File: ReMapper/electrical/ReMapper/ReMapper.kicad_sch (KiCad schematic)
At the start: 50 parts, among them J1 QSPI_Debug, J2 USB_IN, J3 USB_IN_Debug, J4 ESP_UART0, J5 USB_OUT, J6 USB_OUT_Debug, U1 ESP32-S3-WROOM-1-N8R8, U2 RP2040, U3 W25Q128JVE, U4 RT6150B-33GQW, U5 W25Q128JVE, Y1 12MHZ

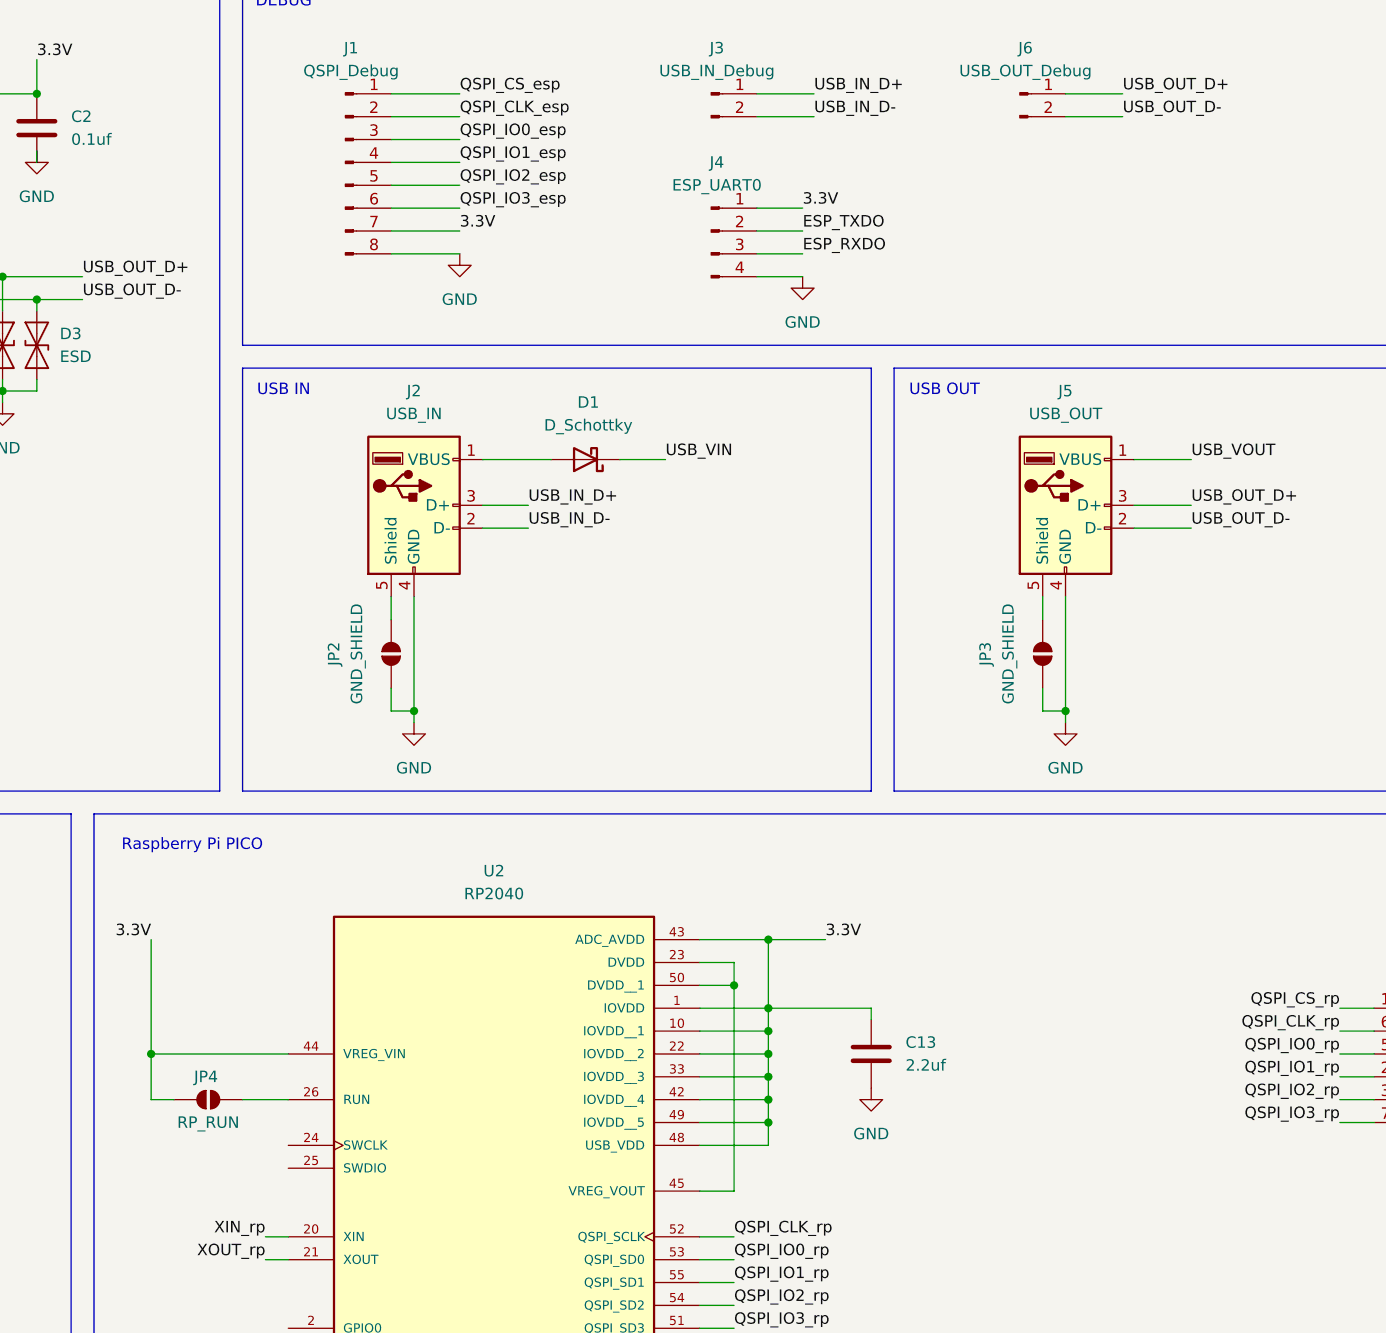
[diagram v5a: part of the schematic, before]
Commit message: split he layout a little
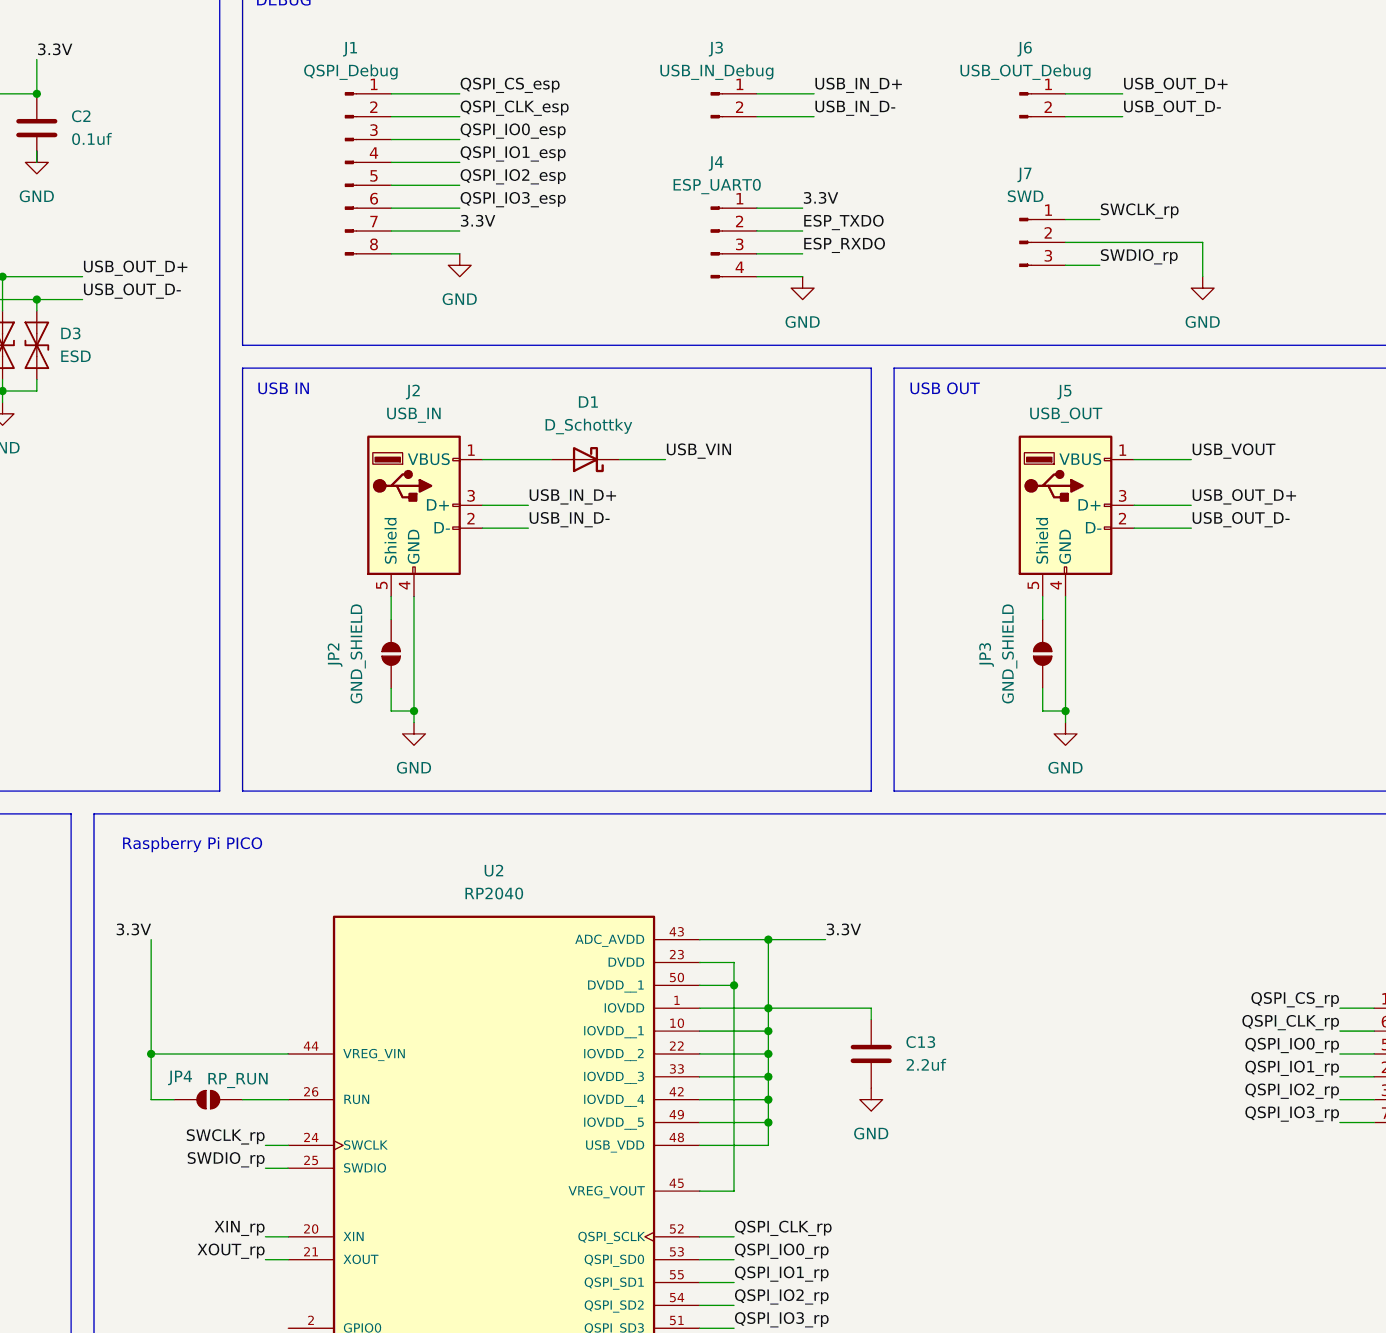
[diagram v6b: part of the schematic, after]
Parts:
- added J7: SWD, Connector_PinHeader_1.00mm:PinHeader_1x03_P1.00mm_Vertical, symbol Connector:Conn_01x03_Pin
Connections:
- net GND: now also J7.2 (Pin_2)
- net SWCLK_rp: now reaches U2.24 (SWCLK)
- net SWCLK_rp: now also J7.1 (Pin_1)
- net SWDIO_rp: now reaches U2.25 (SWDIO)
- net SWDIO_rp: now also J7.3 (Pin_3)
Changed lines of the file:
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@@
 	(wire
 		(pts
+			(xy 245.11 48.26) (xy 248.92 48.26)
+		)
+		(stroke
+			(width 0)
+			(type default)
+		)
+	)
+	(wire
+		(pts
 			(xy 105.41 54.61) (xy 102.87 54.61)
 		)
@@
 	(wire
 		(pts
+			(xy 245.11 45.72) (xy 260.35 45.72)
+		)
+		(stroke
+			(width 0)
+			(type default)
+		)
+	)
+	(wire
+		(pts
 			(xy 236.22 179.07) (xy 236.22 194.31)
 		)
@@
 	(wire
 		(pts
-			(xy 210.82 49.53) (xy 215.9 49.53)
+			(xy 248.92 43.18) (xy 245.11 43.18)
 		)
 		(stroke
@@
 	(wire
 		(pts
+			(xy 260.35 45.72) (xy 260.35 49.53)
+		)
+		(stroke
+			(width 0)
+			(type default)
+		)
+	)
+	(wire
+		(pts
 			(xy 107.95 120.65) (xy 101.6 120.65)
 		)
@@
 	(wire
 		(pts
+			(xy 156.21 146.05) (xy 158.75 146.05)
+		)
+		(stroke
+			(width 0)
+			(type default)
+		)
+	)
+	(wire
+		(pts
 			(xy 101.6 213.36) (xy 106.68 213.36)
 		)
@@
 	(wire
 		(pts
-			(xy 170.18 46.99) (xy 177.8 46.99)
+			(xy 275.59 140.97) (xy 279.4 140.97)
 		)
 		(stroke
@@
 	(wire
 		(pts
-			(xy 275.59 140.97) (xy 279.4 140.97)
+			(xy 46.99 31.75) (xy 72.39 31.75)
 		)
 		(stroke
@@
 	(wire
 		(pts
-			(xy 46.99 31.75) (xy 72.39 31.75)
+			(xy 127 62.23) (xy 127 60.96)
 		)
 		(stroke
@@
 	(wire
 		(pts
-			(xy 127 62.23) (xy 127 60.96)
+			(xy 215.9 49.53) (xy 210.82 49.53)
 		)
 		(stroke
@@
 	(wire
 		(pts
+			(xy 177.8 46.99) (xy 170.18 46.99)
+		)
+		(stroke
+			(width 0)
+			(type default)
+		)
+	)
+	(wire
+		(pts
 			(xy 107.95 200.66) (xy 119.38 200.66)
 		)
@@
 	(wire
 		(pts
+			(xy 156.21 148.59) (xy 158.75 148.59)
+		)
+		(stroke
+			(width 0)
+			(type default)
+		)
+	)
+	(wire
+		(pts
 			(xy 204.47 138.43) (xy 212.09 138.43)
 		)
@@
 		)
 	)
+	(label "SWDIO_rp"
+		(at 248.92 48.26 0)
+		(effects
+			(font
+				(size 1.27 1.27)
+			)
+			(justify left bottom)
+		)
+	)
 	(label "XOUT_rp"
 		(at 156.21 158.75 180)
@@
 		)
 	)
+	(label "SWCLK_rp"
+		(at 248.92 43.18 0)
+		(effects
+			(font
+				(size 1.27 1.27)
+			)
+			(justify left bottom)
+		)
+	)
 	(label "IO8_esp"
 		(at 67.31 64.77 180)
@@
 		)
 	)
+	(label "SWCLK_rp"
+		(at 156.21 146.05 180)
+		(effects
+			(font
+				(size 1.27 1.27)
+			)
+			(justify right bottom)
+		)
+	)
 	(label "QSPI_IO0_esp"
 		(at 177.8 34.29 0)
@@
 		)
 	)
+	(label "SWDIO_rp"
+		(at 156.21 148.59 180)
+		(effects
+			(font
+				(size 1.27 1.27)
+			)
+			(justify right bottom)
+		)
+	)
 	(label "QSPI_IO3_esp"
 		(at 177.8 41.91 0)
@@
 		(dnp no)
 		(property "Reference" "JP4"
-			(at 149.606 138.43 0)
+			(at 146.812 138.43 0)
 			(effects
 				(font
@@
 		)
 		(property "Value" "RP_RUN"
-			(at 149.86 143.51 0)
+			(at 153.162 138.684 0)
 			(effects
 				(font
@@
 	)
 	(symbol
+		(lib_id "power:GND")
+		(at 260.35 49.53 0)
+		(unit 1)
+		(exclude_from_sim no)
+		(in_bom yes)
+		(on_board yes)
+		(dnp no)
+		(fields_autoplaced yes)
+		(property "Reference" "#PWR029"
+			(at 260.35 55.88 0)
+			(effects
+				(font
+					(size 1.27 1.27)
+				)
+				(hide yes)
+			)
+		)
+		(property "Value" "GND"
+			(at 260.35 54.61 0)
+			(effects
+				(font
+					(size 1.27 1.27)
+				)
+			)
+		)
+		(property "Footprint" ""
+			(at 260.35 49.53 0)
+			(effects
+				(font
+					(size 1.27 1.27)
+				)
+				(hide yes)
+			)
+		)
+		(property "Datasheet" ""
+			(at 260.35 49.53 0)
+			(effects
+				(font
+					(size 1.27 1.27)
+				)
+				(hide yes)
+			)
+		)
+		(property "Description" "Power symbol creates a global label with name \"GND\" , ground"
+			(at 260.35 49.53 0)
+			(effects
+				(font
+					(size 1.27 1.27)
+				)
+				(hide yes)
+			)
+		)
+		(pin "1"
+		)
+		(instances
+			(project "ReMapper"
+				(path "/facd47ac-9f29-4b3c-ae50-ce7a688e305d"
+					(reference "#PWR029")
+					(unit 1)
+				)
+			)
+		)
+	)
+	(symbol
 		(lib_id "Device:L")
 		(at 119.38 204.47 0)
@@
 					(unit 1)
 				)
+			)
+		)
+	)
+	(symbol
+		(lib_id "Connector:Conn_01x03_Pin")
+		(at 240.03 45.72 0)
+		(unit 1)
+		(exclude_from_sim no)
+		(in_bom yes)
+		(on_board yes)
+		(dnp no)
+		(property "Reference" "J7"
+			(at 240.665 38.1 0)
+			(effects
+				(font
+					(size 1.27 1.27)
+				)
+			)
+		)
+		(property "Value" "SWD"
+			(at 240.665 40.64 0)
+			(effects
+				(font
+					(size 1.27 1.27)
+				)
+			)
+		)
+		(property "Footprint" "Connector_PinHeader_1.00mm:PinHeader_1x03_P1.00mm_Vertical"
+			(at 240.03 45.72 0)
+			(effects
+				(font
+					(size 1.27 1.27)
+				)
+				(hide yes)
+			)
+		)
+		(property "Datasheet" "~"
+			(at 240.03 45.72 0)
+			(effects
+				(font
+					(size 1.27 1.27)
+				)
+				(hide yes)
+			)
+		)
+		(property "Description" "Generic connector, single row, 01x03, script generated"
+			(at 240.03 45.72 0)
+			(effects
+				(font
+					(size 1.27 1.27)
+				)
+				(hide yes)
+			)
+		)
+		(pin "3"
+		)
+		(pin "2"
+		)
+		(pin "1"
+		)
+		(instances
+			(project ""
+				(path "/facd47ac-9f29-4b3c-ae50-ce7a688e305d"
+					(reference "J7")
+					(unit 1)
+				)

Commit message: rough placements
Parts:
- renumbered D6 to 33V_led, J1 to ESP_QSPI, J4 to ESP_UART0, J7 to RP_SWD, J3 to USB_IN, J6 to USB_OUT, D7 to USB_led, D9 to esp_led, D8 to rp_led
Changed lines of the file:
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@@
 		(dnp no)
 		(fields_autoplaced yes)
-		(property "Reference" "D7"
+		(property "Reference" "USB_led"
 			(at 335.28 42.2274 90)
 			(effects
@@
 			(project "ReMapper"
 				(path "/facd47ac-9f29-4b3c-ae50-ce7a688e305d"
-					(reference "D7")
+					(reference "USB_led")
 					(unit 1)
 				)
@@
 		(dnp no)
 		(fields_autoplaced yes)
-		(property "Reference" "J3"
+		(property "Reference" "USB_IN"
 			(at 206.375 24.13 0)
 			(effects
@@
 			(project ""
 				(path "/facd47ac-9f29-4b3c-ae50-ce7a688e305d"
-					(reference "J3")
+					(reference "USB_IN")
 					(unit 1)
 				)
@@
 		(dnp no)
 		(fields_autoplaced yes)
-		(property "Reference" "D6"
+		(property "Reference" "33V_led"
 			(at 314.96 42.2274 90)
 			(effects
@@
 			(project ""
 				(path "/facd47ac-9f29-4b3c-ae50-ce7a688e305d"
-					(reference "D6")
+					(reference "33V_led")
 					(unit 1)
 				)
@@
 		(on_board yes)
 		(dnp no)
-		(property "Reference" "J4"
+		(property "Reference" "ESP_UART0"
 			(at 206.375 36.83 0)
 			(effects
@@
 			(project ""
 				(path "/facd47ac-9f29-4b3c-ae50-ce7a688e305d"
-					(reference "J4")
+					(reference "ESP_UART0")
 					(unit 1)
 				)
@@
 		(dnp no)
 		(fields_autoplaced yes)
-		(property "Reference" "D9"
+		(property "Reference" "esp_led"
 			(at 386.08 42.2274 90)
 			(effects
@@
 			(project "ReMapper"
 				(path "/facd47ac-9f29-4b3c-ae50-ce7a688e305d"
-					(reference "D9")
+					(reference "esp_led")
 					(unit 1)
 				)
@@
 		(dnp no)
 		(fields_autoplaced yes)
-		(property "Reference" "J1"
+		(property "Reference" "ESP_QSPI"
 			(at 165.735 24.13 0)
 			(effects
@@
 			(project ""
 				(path "/facd47ac-9f29-4b3c-ae50-ce7a688e305d"
-					(reference "J1")
+					(reference "ESP_QSPI")
 					(unit 1)
 				)
@@
 		(dnp no)
 		(fields_autoplaced yes)
-		(property "Reference" "D8"
+		(property "Reference" "rp_led"
 			(at 363.22 42.2274 90)
 			(effects
@@
 			(project "ReMapper"
 				(path "/facd47ac-9f29-4b3c-ae50-ce7a688e305d"
-					(reference "D8")
+					(reference "rp_led")
 					(unit 1)
 				)
@@
 		(dnp no)
 		(fields_autoplaced yes)
-		(property "Reference" "J6"
+		(property "Reference" "USB_OUT"
 			(at 240.665 24.13 0)
 			(effects
@@
 			(project "ReMapper"
 				(path "/facd47ac-9f29-4b3c-ae50-ce7a688e305d"
-					(reference "J6")
+					(reference "USB_OUT")
 					(unit 1)
 				)
@@
 		(on_board yes)
 		(dnp no)
-		(property "Reference" "J7"
+		(property "Reference" "RP_SWD"
 			(at 240.665 38.1 0)
 			(effects
@@
 			(project ""
 				(path "/facd47ac-9f29-4b3c-ae50-ce7a688e305d"
-					(reference "J7")
+					(reference "RP_SWD")
 					(unit 1)
 				)

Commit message: layout half done, might needs a remake
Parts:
- renumbered 33V_led to 33V_led1, ESP_QSPI to ESP_QSPI1, RP_SWD to RP_SWD1, USB_IN to USB_IN1, USB_OUT to USB_OUT1, USB_led to USB_led1, esp_led to esp_led1, rp_led to rp_led1
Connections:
- net USB_IN_D+: now also U2.46 (USB_DM)
- net USB_IN_D-: now also U2.47 (USB_DP)
- net USB_OUT_D+: no longer U2.46 (USB_DM)
- net USB_OUT_D-: no longer U2.47 (USB_DP)
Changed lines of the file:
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@@
 		)
 	)
-	(label "USB_OUT_D+"
+	(label "USB_IN_D+"
 		(at 208.28 173.99 0)
 		(effects
@@
 		)
 	)
-	(label "USB_OUT_D-"
+	(label "USB_IN_D-"
 		(at 208.28 176.53 0)
 		(effects
@@
 		(dnp no)
 		(fields_autoplaced yes)
-		(property "Reference" "USB_led"
+		(property "Reference" "USB_led1"
 			(at 335.28 42.2274 90)
 			(effects
@@
 			(project "ReMapper"
 				(path "/facd47ac-9f29-4b3c-ae50-ce7a688e305d"
-					(reference "USB_led")
+					(reference "USB_led1")
 					(unit 1)
 				)
@@
 		(dnp no)
 		(fields_autoplaced yes)
-		(property "Reference" "USB_IN"
+		(property "Reference" "USB_IN1"
 			(at 206.375 24.13 0)
 			(effects
@@
 			(project ""
 				(path "/facd47ac-9f29-4b3c-ae50-ce7a688e305d"
-					(reference "USB_IN")
+					(reference "USB_IN1")
 					(unit 1)
 				)
@@
 		(dnp no)
 		(fields_autoplaced yes)
-		(property "Reference" "33V_led"
+		(property "Reference" "33V_led1"
 			(at 314.96 42.2274 90)
 			(effects
@@
 			(project ""
 				(path "/facd47ac-9f29-4b3c-ae50-ce7a688e305d"
-					(reference "33V_led")
+					(reference "33V_led1")
 					(unit 1)
 				)
@@
 		(dnp no)
 		(fields_autoplaced yes)
-		(property "Reference" "esp_led"
+		(property "Reference" "esp_led1"
 			(at 386.08 42.2274 90)
 			(effects
@@
 			(project "ReMapper"
 				(path "/facd47ac-9f29-4b3c-ae50-ce7a688e305d"
-					(reference "esp_led")
+					(reference "esp_led1")
 					(unit 1)
 				)
@@
 		(dnp no)
 		(fields_autoplaced yes)
-		(property "Reference" "ESP_QSPI"
+		(property "Reference" "ESP_QSPI1"
 			(at 165.735 24.13 0)
 			(effects
@@
 			(project ""
 				(path "/facd47ac-9f29-4b3c-ae50-ce7a688e305d"
-					(reference "ESP_QSPI")
+					(reference "ESP_QSPI1")
 					(unit 1)
 				)
@@
 		(dnp no)
 		(fields_autoplaced yes)
-		(property "Reference" "rp_led"
+		(property "Reference" "rp_led1"
 			(at 363.22 42.2274 90)
 			(effects
@@
 			(project "ReMapper"
 				(path "/facd47ac-9f29-4b3c-ae50-ce7a688e305d"
-					(reference "rp_led")
+					(reference "rp_led1")
 					(unit 1)
 				)
@@
 		(dnp no)
 		(fields_autoplaced yes)
-		(property "Reference" "USB_OUT"
+		(property "Reference" "USB_OUT1"
 			(at 240.665 24.13 0)
 			(effects
@@
 			(project "ReMapper"
 				(path "/facd47ac-9f29-4b3c-ae50-ce7a688e305d"
-					(reference "USB_OUT")
+					(reference "USB_OUT1")
 					(unit 1)
 				)
@@
 		(on_board yes)
 		(dnp no)
-		(property "Reference" "RP_SWD"
+		(property "Reference" "RP_SWD1"
 			(at 240.665 38.1 0)
 			(effects
@@
 			(project ""
 				(path "/facd47ac-9f29-4b3c-ae50-ce7a688e305d"
-					(reference "RP_SWD")
+					(reference "RP_SWD1")
 					(unit 1)
 				)
